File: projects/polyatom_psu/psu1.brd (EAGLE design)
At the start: 49.5 x 97.5 mm, 33 parts

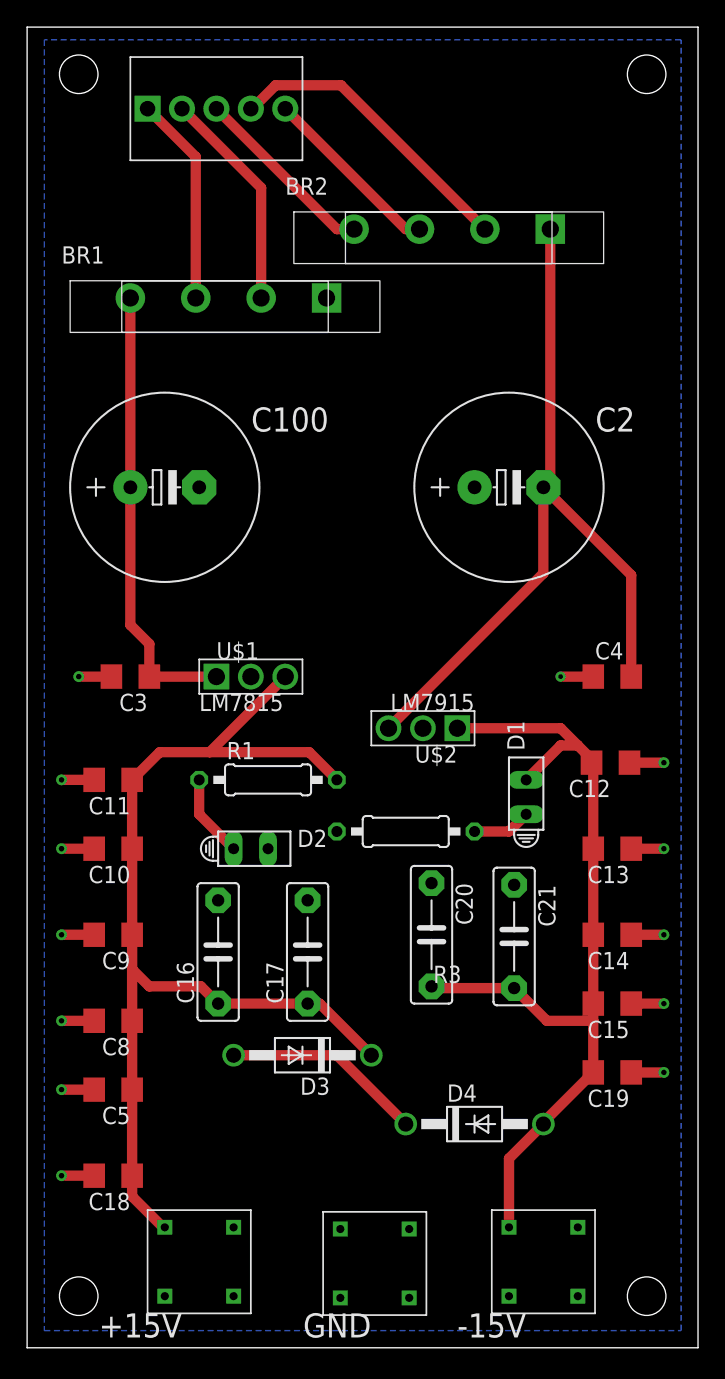
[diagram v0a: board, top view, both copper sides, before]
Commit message: added top and bottom pour, caps renamed
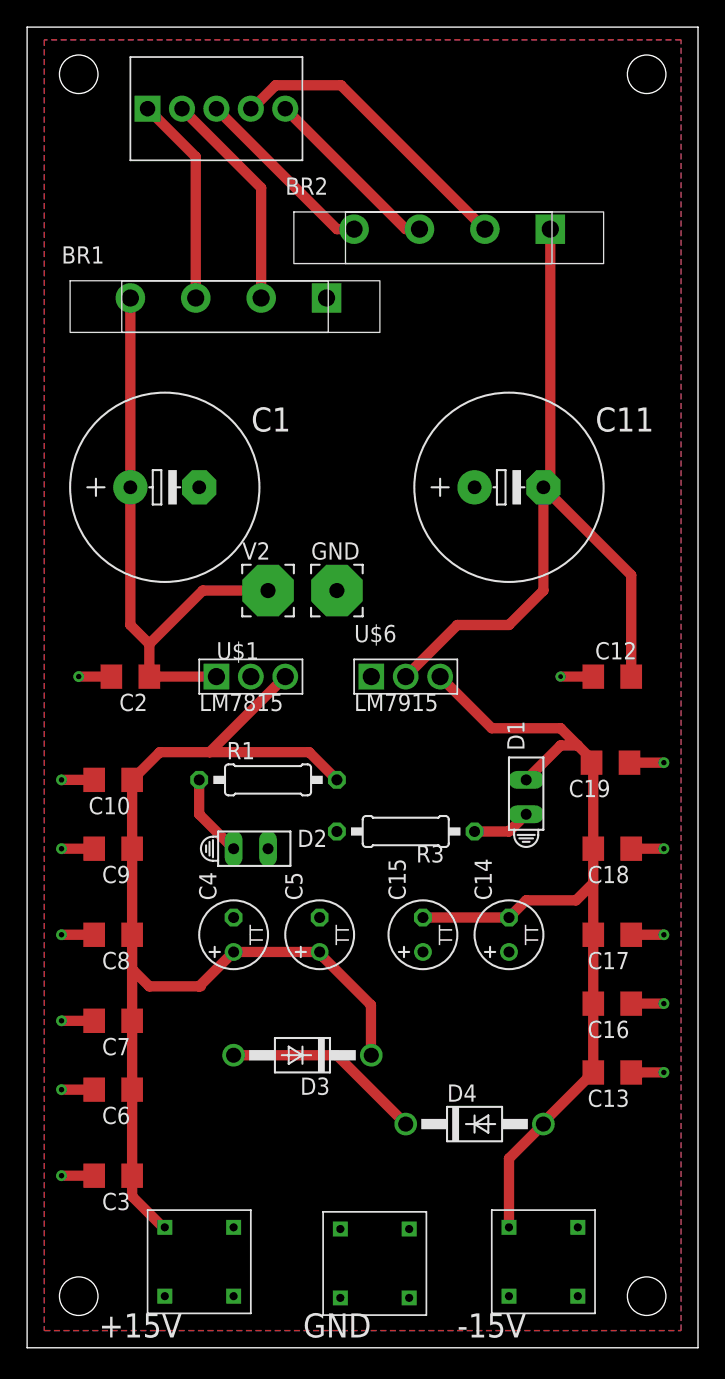
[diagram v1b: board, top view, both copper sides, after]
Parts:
- removed C20, C21: 10u, capacitor-wima:C7.5B3
- removed U$2: LM7915, STM_Library:TO-220
- added C6, C7: 100n, eagle-ltspice:C1206
- added GND, V2: (no value), wirepad:3,81/1,1
- added U$6: LM7915, STM_Library:TO-220
- C11: value 100n -> 1000u; device eagle-ltspice:C1206 -> rcl:E5-13
- C12: value 100n -> 2.2u; device eagle-ltspice:C1206 -> rcl:C1206
- C13: value 100n -> 1u; device eagle-ltspice:C1206 -> rcl:C1206
- C14, C15, C5: value 100n -> (none); device eagle-ltspice:C1206 -> rcl:TT2D5
- C16, C17: value 10u -> 100n; device capacitor-wima:C7.5B3 -> eagle-ltspice:C1206
- C18: device rcl:C1206 -> eagle-ltspice:C1206
- C19: value 1u -> 100n; device rcl:C1206 -> eagle-ltspice:C1206
- C2: value 1000u -> 0.22u; device rcl:E5-13 -> rcl:C1206
- C3: value 0.22u -> 100n
- C4: value 2.2u -> (none); device rcl:C1206 -> rcl:TT2D5
- moved C18 44.0 mm to (43.2, 36.8)
- moved C3 36.9 mm to (6.35, 12.7)
- moved C11 36.3 mm to (35.6, 63.5), turned to 0 degrees
- moved C4 33.8 mm to (15.2, 30.5), turned to 90 degrees
- moved C2 31.2 mm to (7.62, 49.5), turned to 180 degrees
- moved C16 29.3 mm to (43.2, 25.4), turned to 180 degrees
- moved C19 22.9 mm to (43.1, 43.2)
- moved C17 22.5 mm to (43.2, 30.5), turned to 180 degrees
- moved C5 19.1 mm to (21.6, 30.5), turned to 90 degrees
- moved C13 16.5 mm to (43.2, 20.3)
- moved C15 14.9 mm to (29.2, 30.5), turned to 90 degrees
- moved C14 7.62 mm to (35.6, 30.5), turned to 90 degrees
- moved C12 6.35 mm to (43.2, 49.5), turned to 0 degrees
- moved C8 6.35 mm to (6.35, 30.5)
- moved C9 6.35 mm to (6.35, 36.8)
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- renumbered C100 to C1
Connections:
- net +15V: now also C3.1, C4.+, C5.+, C6.1, C7.1; no longer C11.1, C16.1, C17.1, C18.1, C5.1
- net -15V: now also C14.-, C15.-, C16.2, C17.2, C18.2, U$6.P$3; no longer C12.2, C14.2, C15.2, C20.2, C21.2, U$2.P$1
- net GND: now also C11.+, C14.+, C15.+, C16.1, C17.1, C18.1, C2.2, C4.-, C5.-, C6.2, C7.2, GND.1, U$6.P$1; no longer C11.2, C14.1, C15.1, C16.2, C17.2, C18.2, C2.+, C20.1, C21.1, C4.1, C5.2, U$2.P$2
- net NEG: now also C11.-, C12.2, U$6.P$2; no longer C2.-, C4.2, U$2.P$3
- net POS: now also C2.1, V2.1; no longer C3.1
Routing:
- net POS: track 33.5 -> 43.9 mm
- net +15V: track 80.0 -> 84.7 mm
- net -15V: track 66.1 -> 69.7 mm
- net NEG: track 58.4 -> 56.3 mm
- added copper zone on layer 1, net N$1

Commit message: added text to the top and bottom of board
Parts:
- moved U$6 5.08 mm to (30.5, 49.5), turned to 270 degrees
- moved C12 5.08 mm to (38.1, 49.5), turned to 180 degrees
- moved C11 2.54 mm to (35.6, 66.0)
- moved C1 1.27 mm to (10.2, 64.8)
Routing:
- net GND: track 60.1 -> 45.3 mm
- net NEG: track 56.3 -> 43.3 mm
- net -15V: track 69.7 -> 68.6 mm
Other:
- board text added: "Polyatom STM 2019"
